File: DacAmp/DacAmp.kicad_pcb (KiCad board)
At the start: 4 copper layers, 110 parts, among them J1 AudioPlug3, J2 USB_B, U1 PCM2906C, U10 TLV70237_SOT23-5, U11 TLV61046ADB, U12 NE5532, U13 LM2941LD_NOPB, U2 NE5532, U3 NE5532, U4 NE5532, U5 NE5532, U6 NE5532, U7 NE5532, U8 NE5532, U9 NE5532, Y1 12MHz

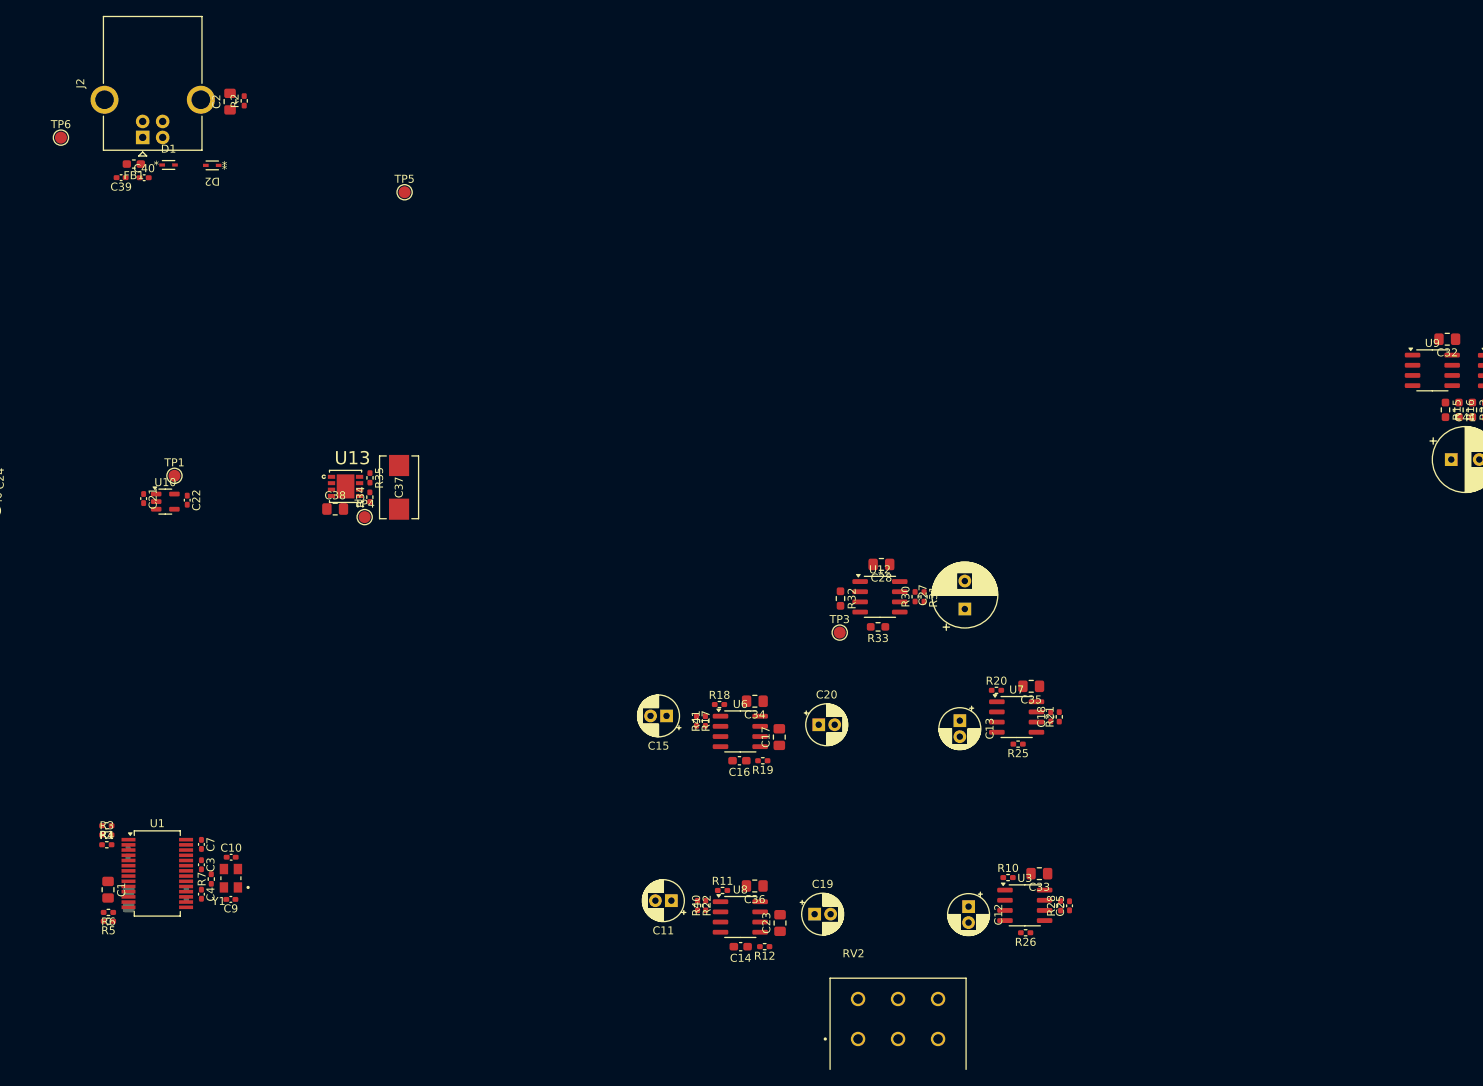
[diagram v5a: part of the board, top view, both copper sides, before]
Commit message: add potential edge cuts
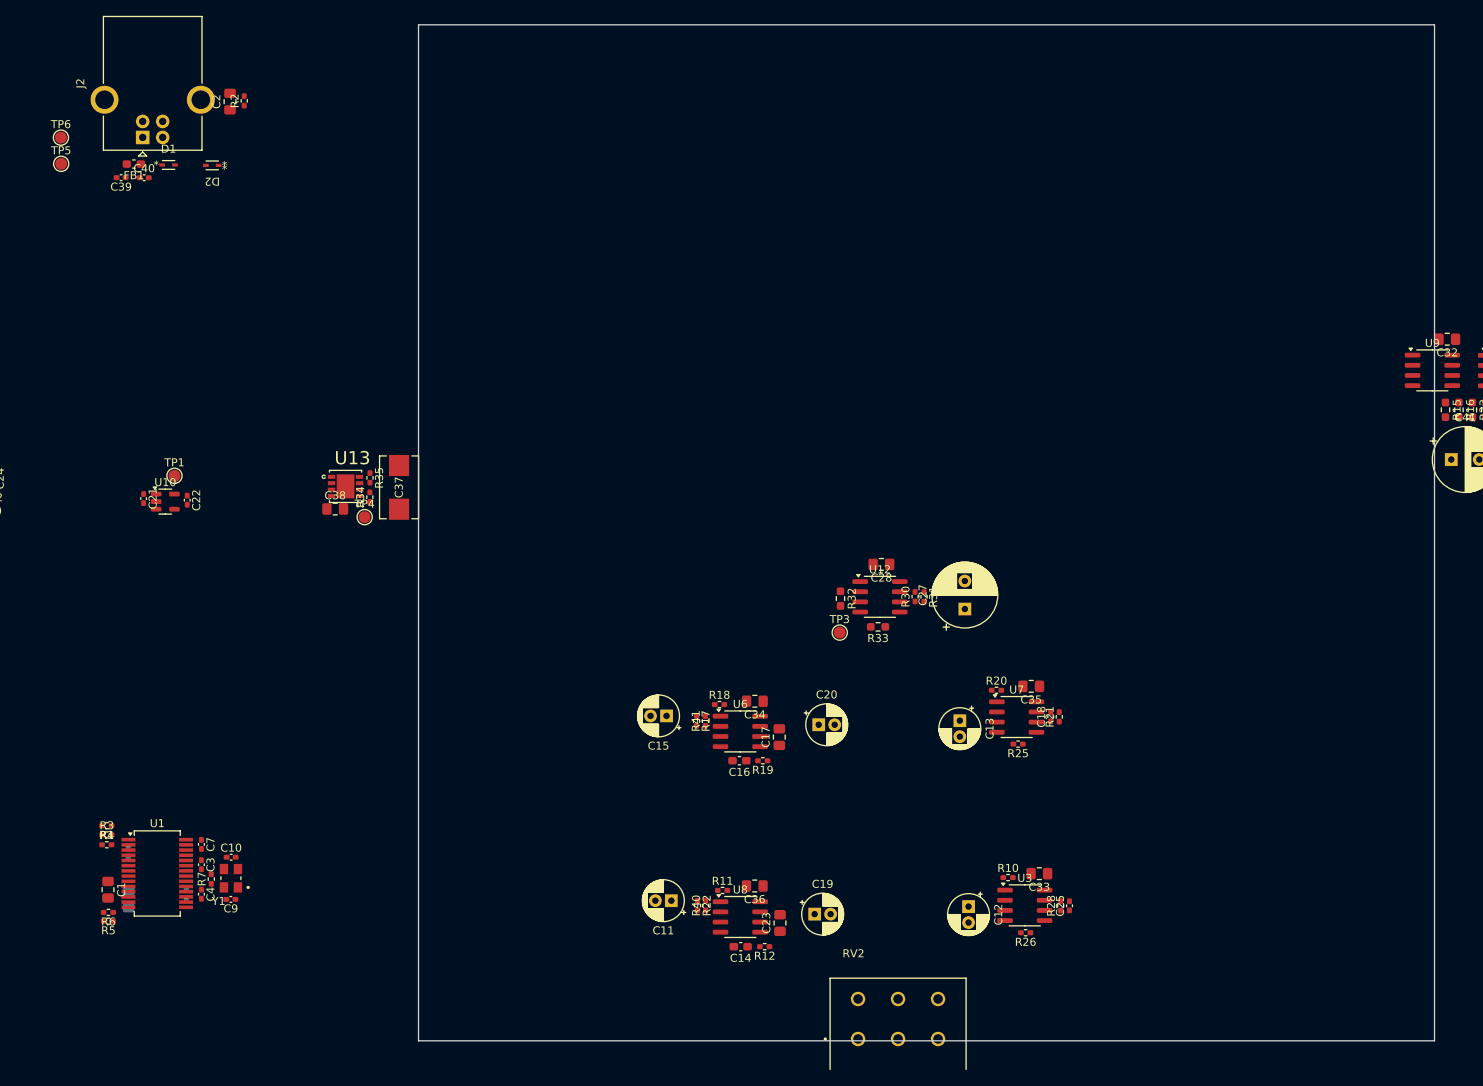
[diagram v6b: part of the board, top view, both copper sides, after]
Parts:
- moved TP5 43.1 mm to (33.3, 56.7)
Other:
- board outline added: 127 x 127 mm
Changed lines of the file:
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@@
 	(footprint "TestPoint:TestPoint_Pad_D1.5mm"
 		(layer "F.Cu")
-		(at 76.24 60.3)
+		(at 33.314 56.744)
 		(descr "SMD pad as test Point, diameter 1.5mm")
 		(tags "test point SMD pad")
@@
 		)
 	)
+	(gr_rect
+		(start 77.978 39.37)
+		(end 204.978 166.37)
+		(stroke
+			(width 0.05)
+			(type default)
+		)
+		(fill none)
+		(layer "Edge.Cuts")
+	)
 )

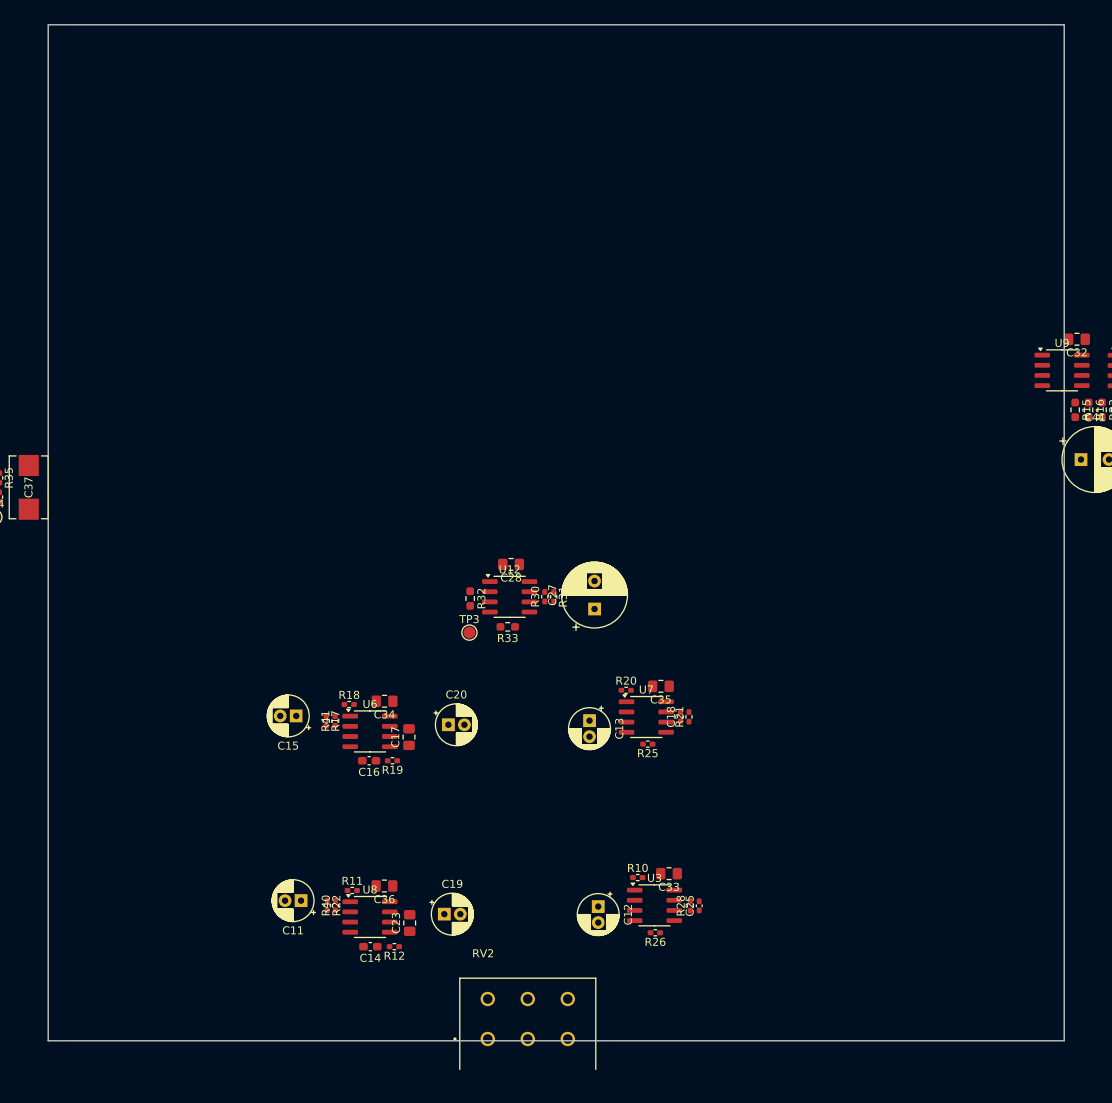
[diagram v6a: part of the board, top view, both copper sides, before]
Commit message: add 3d models
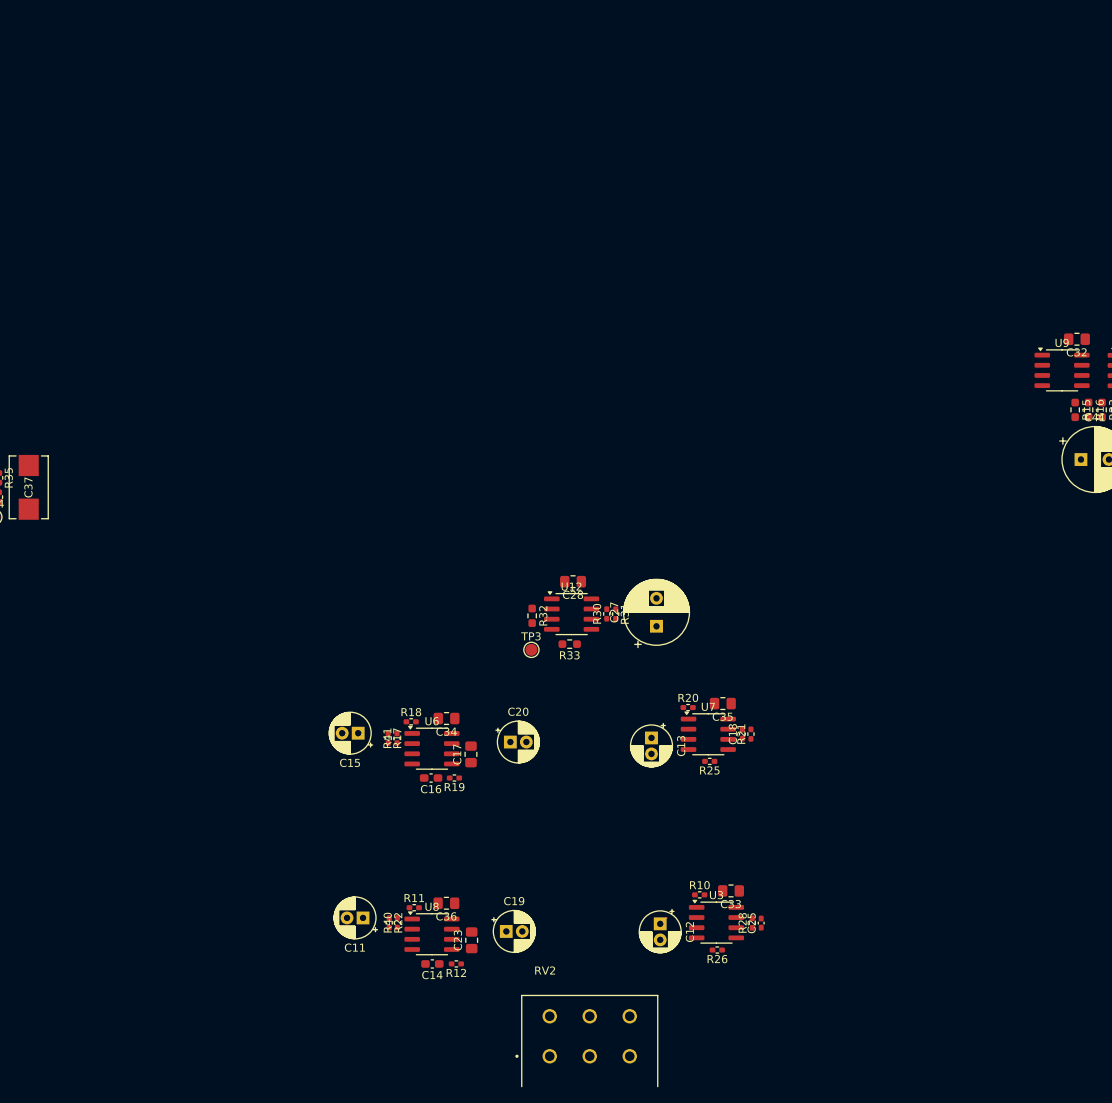
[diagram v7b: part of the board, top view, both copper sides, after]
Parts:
- moved C12 8.04 mm to (154.5, 151.8)
- moved C13 8.04 mm to (153.4, 128.5)
- moved C20 8.04 mm to (135.7, 129.0)
- moved C28 8.04 mm to (143.6, 109.0)
- moved C35 8.04 mm to (162.3, 124.2)
- moved R20 8.04 mm to (158.0, 124.7)
- moved R21 8.04 mm to (165.8, 128.0)
- moved R30 8.04 mm to (147.8, 113.0)
- moved TP3 8.04 mm to (138.4, 117.5)
- moved R12 8.04 mm to (129.0, 156.8)
- moved R32 8.04 mm to (138.5, 113.2)
- moved RV2 8.04 mm to (140.7, 168.3)
- moved U3 8.04 mm to (161.5, 151.6)
- moved U7 8.04 mm to (160.5, 128.1)
- moved C14 8.04 mm to (126.0, 156.8)
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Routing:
- net /Preamp/VC_INR: track 0.00 -> 1.15 mm
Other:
- board outline removed

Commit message: finish rough floor plan
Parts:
- added H1: MountingHole_Pad, MountingHole:MountingHole_2.7mm_M2.5_ISO7380_Pad, F.Cu at (40.3, 32.8)
- added H2: MountingHole_Pad, MountingHole:MountingHole_2.7mm_M2.5_ISO7380_Pad, F.Cu at (135.5, 32.8)
- added H3: MountingHole_Pad, MountingHole:MountingHole_2.7mm_M2.5_ISO7380_Pad, F.Cu at (40.3, 119.1)
- added H4: MountingHole_Pad, MountingHole:MountingHole_2.7mm_M2.5_ISO7380_Pad, F.Cu at (135.5, 119.1)
- moved C29 142.7 mm to (106.2, 89.5)
- moved C30 142.7 mm to (96.6, 89.4)
- moved C42 142.7 mm to (97.6, 104.8)
- moved R13 142.7 mm to (100.0, 98.4)
- moved R14 142.7 mm to (101.5, 98.4)
- moved R37 142.7 mm to (104.6, 105.4)
- moved R8 142.7 mm to (96.9, 98.4)
- moved R9 142.7 mm to (98.4, 98.4)
- moved U2 142.7 mm to (104.4, 93.3)
- moved U4 142.7 mm to (94.9, 93.3)
- moved D4 131.5 mm to (108.9, 119.7), turned to -90 degrees
- moved J1 118.6 mm to (115.4, 117.6), turned to 180 degrees
- moved R12 113.7 mm to (35.3, 92.4), turned to 90 degrees
- moved C14 113.0 mm to (35.3, 89.4), turned to 90 degrees
- moved R27 111.5 mm to (116.1, 48.3), turned to 180 degrees
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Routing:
- net /Preamp/VC_INR: track 1.15 -> 0.00 mm
- added copper zone on In1.Cu, net GND
- added copper zone on In2.Cu, net GND
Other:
- board outline added: 110.5 x 101.6 mm
